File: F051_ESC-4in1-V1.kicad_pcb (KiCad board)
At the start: 4 copper layers, 41 x 40 mm, 136 parts, among them J1 Conn_01x02, J2 Conn_01x04, J3 Conn_01x04, J4 Conn_01x03, J5 Conn_01x04, J6 Conn_01x03, J7 Conn_01x03, J8 Conn_01x03, Q1 TPHR8504PL, Q10 TPHR8504PL, Q11 TPHR8504PL, Q12 TPHR8504PL, Q2 TPHR8504PL, Q3 TPHR8504PL, Q4 TPHR8504PL, Q5 TPHR8504PL, Q6 TPHR8504PL, Q7 TPHR8504PL, Q8 TPHR8504PL, Q9 TPHR8504PL, U1 FD6288Q, U2 STM32F051K6Ux, U3 L78L12_SOT89, U4 LP2985-3.3, U5 INA139, U6 FD6288Q, U7 OPA340NA, U8 STM32F051K6Ux

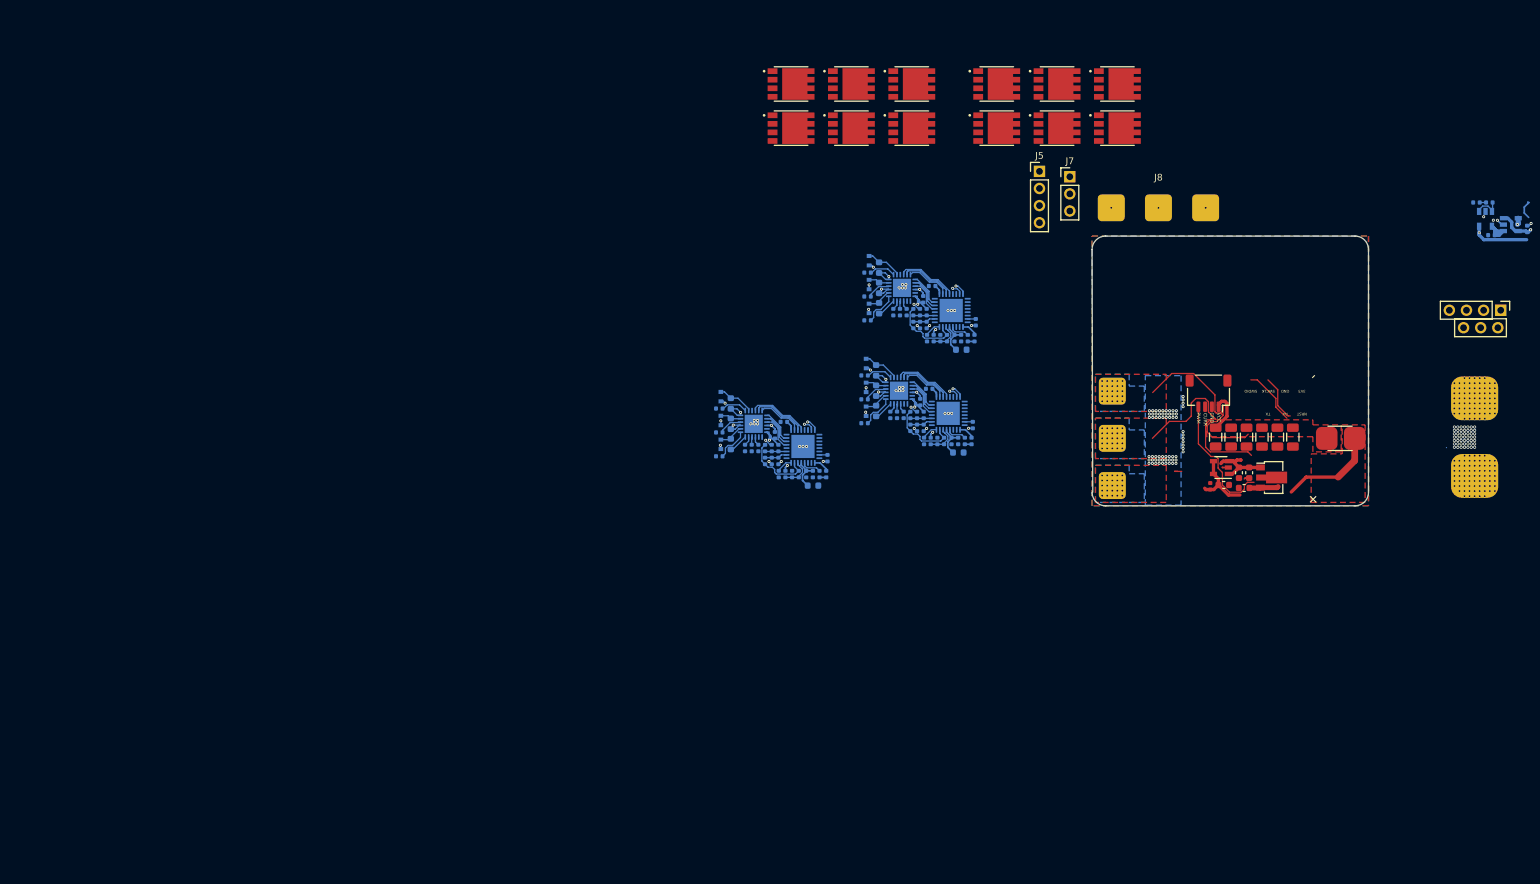
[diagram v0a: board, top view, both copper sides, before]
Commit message: Added the rest of the phases and their associated components
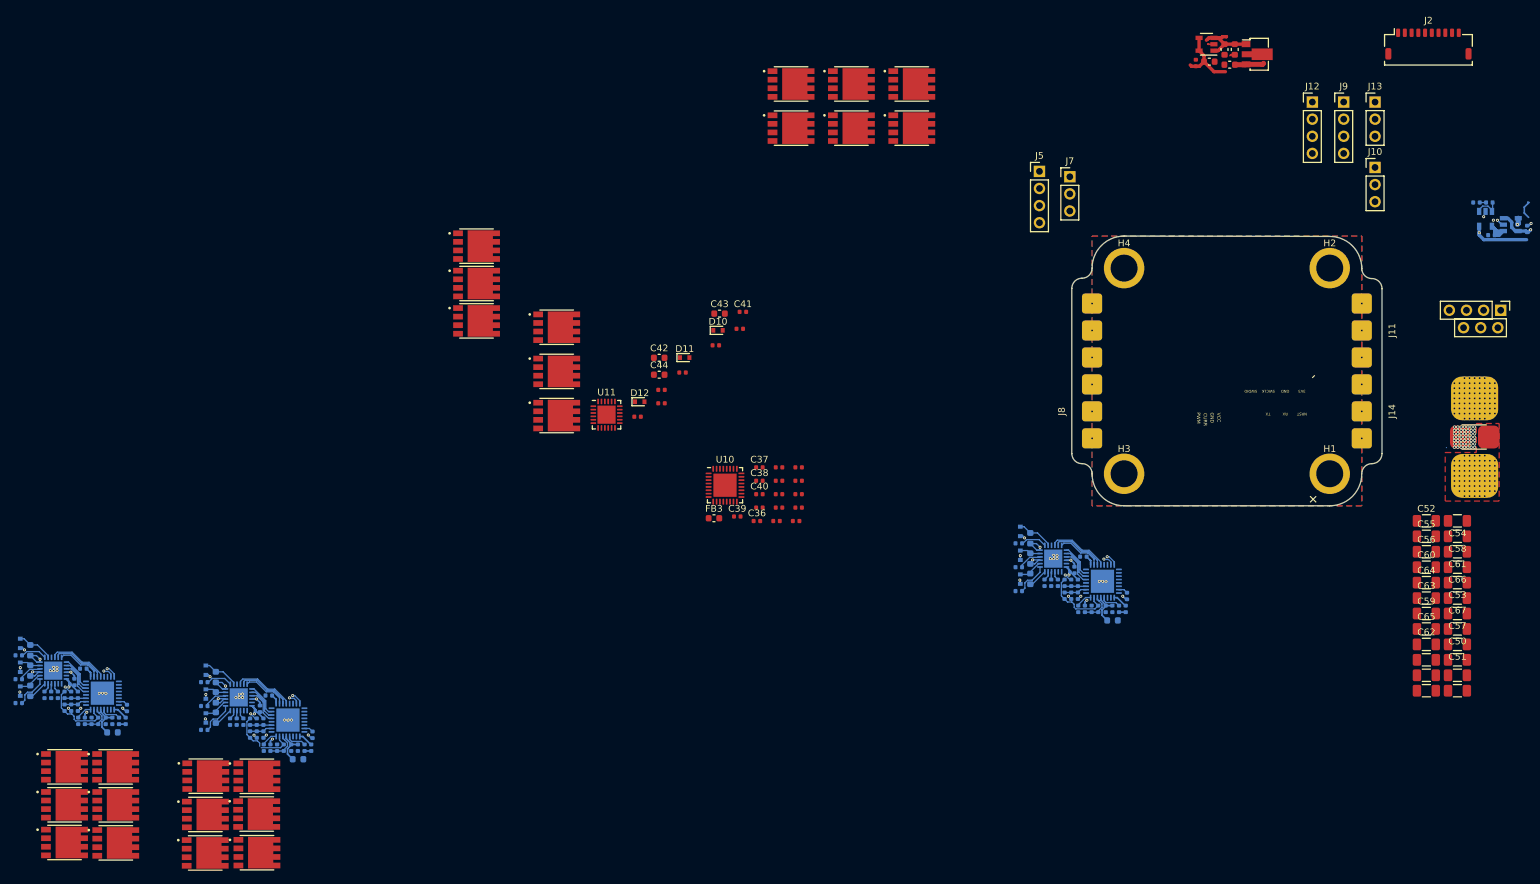
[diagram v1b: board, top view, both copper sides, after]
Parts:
- removed the C1 at (179.6, 85.3)
- removed the C11 at (172.0, 79.5)
- removed the C12 at (165.4, 77.8)
- removed the C13 at (165.4, 74.8)
- removed the C14 at (165.4, 80.8)
- removed the C15 at (178.6, 85.3)
- removed the C2 at (173.3, 77.6)
- removed the C3 at (176.6, 85.3)
- removed the C6 at (177.6, 85.3)
- removed the D2 at (163.9, 77.3)
- removed the D3 at (163.9, 73.8)
- removed the D4 at (163.9, 80.9)
- removed the FB1 at (177.6, 87.0)
- removed the R10 at (168.5, 81.4)
- removed the R11 at (163.7, 82.7)
- removed the R12 at (169.5, 81.4)
- removed the R13 at (171.5, 81.4)
- removed the R14 at (170.5, 81.4)
- removed the R15 at (171.5, 83.3)
- removed the R16 at (172.5, 81.4)
- removed the R17 at (170.5, 83.3)
- removed the R18 at (174.5, 85.3)
- removed the R19 at (175.5, 85.3)
- removed the R20 at (172.5, 83.3)
- removed the R21 at (173.5, 85.3)
- removed the R23 at (179.8, 82.9)
- removed the R24 at (172.5, 85.3)
- removed the R7 at (163.7, 75.6)
- removed the R8 at (167.5, 81.4)
- removed the R9 at (163.7, 79.1)
- removed the U1 at (168.8, 77.8)
- removed the U2 at (176.1, 81.2)
- added C32: 0.1uF, Capacitor_SMD:C_0402_1005Metric, B.Cu at (95.6, 120.1)
- added C33: 0.1uF, Capacitor_SMD:C_0603_1608Metric, B.Cu at (89.0, 115.4)
- added C34: 0.1uF, Capacitor_SMD:C_0603_1608Metric, B.Cu at (89.0, 118.4)
- added C35: 0.1uF, Capacitor_SMD:C_0603_1608Metric, B.Cu at (89.0, 121.4)
- added C36: 10nF, Capacitor_SMD:C_0402_1005Metric, F.Cu at (169.3, 92.3)
- added C37: 1uF, Capacitor_SMD:C_0402_1005Metric, F.Cu at (169.7, 84.3)
- added C38: 0.1uF, Capacitor_SMD:C_0402_1005Metric, F.Cu at (169.7, 86.3)
- added C39: 0.1uF, Capacitor_SMD:C_0402_1005Metric, F.Cu at (166.4, 91.6)
- added C40: 0.1uF, Capacitor_SMD:C_0402_1005Metric, F.Cu at (169.7, 88.3)
- added C41: 0.1uF, Capacitor_SMD:C_0402_1005Metric, F.Cu at (167.2, 61.2)
- added C42: 0.1uF, Capacitor_SMD:C_0603_1608Metric, F.Cu at (154.8, 68.0)
- added C43: 0.1uF, Capacitor_SMD:C_0603_1608Metric, F.Cu at (163.8, 61.5)
- added C44: 0.1uF, Capacitor_SMD:C_0603_1608Metric, F.Cu at (154.8, 70.6)
- added C45: 10nF, Capacitor_SMD:C_0402_1005Metric, B.Cu at (100.2, 125.9)
- added C46: 1uF, Capacitor_SMD:C_0402_1005Metric, B.Cu at (101.2, 125.9)
- added C47: 0.1uF, Capacitor_SMD:C_0402_1005Metric, B.Cu at (103.2, 125.9)
- added C48: 0.1uF, Capacitor_SMD:C_0402_1005Metric, B.Cu at (96.9, 118.1)
- added C49: 0.1uF, Capacitor_SMD:C_0402_1005Metric, B.Cu at (102.2, 125.9)
- added C50: 0.1uF, Capacitor_SMD:C_1206_3216Metric, F.Cu at (273.2, 108.3)
- added C51: 0.1uF, Capacitor_SMD:C_1206_3216Metric, F.Cu at (273.2, 110.6)
- added C52: 0.1uF, Capacitor_SMD:C_1206_3216Metric, F.Cu at (268.6, 92.2)
- added C53: 0.1uF, Capacitor_SMD:C_1206_3216Metric, F.Cu at (273.2, 101.4)
- added C54: 0.1uF, Capacitor_SMD:C_1206_3216Metric, F.Cu at (273.2, 92.2)
- added C55: 0.1uF, Capacitor_SMD:C_1206_3216Metric, F.Cu at (268.6, 94.5)
- added C56: 0.1uF, Capacitor_SMD:C_1206_3216Metric, F.Cu at (268.6, 96.8)
- added C57: 0.1uF, Capacitor_SMD:C_1206_3216Metric, F.Cu at (273.2, 106.0)
- added C58: 0.1uF, Capacitor_SMD:C_1206_3216Metric, F.Cu at (273.2, 94.5)
- added C59: 0.1uF, Capacitor_SMD:C_1206_3216Metric, F.Cu at (268.6, 106.0)
- added C60: 0.1uF, Capacitor_SMD:C_1206_3216Metric, F.Cu at (268.6, 99.1)
- added C61: 0.1uF, Capacitor_SMD:C_1206_3216Metric, F.Cu at (273.2, 96.8)
- added C62: 0.1uF, Capacitor_SMD:C_1206_3216Metric, F.Cu at (268.6, 110.6)
- added C63: 0.1uF, Capacitor_SMD:C_1206_3216Metric, F.Cu at (268.6, 103.7)
- added C64: 0.1uF, Capacitor_SMD:C_1206_3216Metric, F.Cu at (268.6, 101.4)
- added C65: 0.1uF, Capacitor_SMD:C_1206_3216Metric, F.Cu at (268.6, 108.3)
- added C66: 0.1uF, Capacitor_SMD:C_1206_3216Metric, F.Cu at (273.2, 99.1)
- added C67: 0.1uF, Capacitor_SMD:C_1206_3216Metric, F.Cu at (273.2, 103.7)
- added D10: 250V, Diode_SMD:D_SOD-523, F.Cu at (163.5, 64.0)
- added D11: 250V, Diode_SMD:D_SOD-523, F.Cu at (158.6, 68.0)
- added D12: 250V, Diode_SMD:D_SOD-523, F.Cu at (151.9, 74.6)
- added D7: 250V, Diode_SMD:D_SOD-523, B.Cu at (87.6, 114.4)
- added D8: 250V, Diode_SMD:D_SOD-523, B.Cu at (87.6, 117.9)
- added D9: 250V, Diode_SMD:D_SOD-523, B.Cu at (87.6, 121.5)
- added FB3: 100@100MHz, Inductor_SMD:L_0603_1608Metric, F.Cu at (162.9, 91.8)
- added FB4: 100@100MHz, Inductor_SMD:L_0603_1608Metric, B.Cu at (101.2, 127.6)
- added H1: MountingHole_Pad, MountingHole:MountingHole_2.7mm_Pad, F.Cu at (254.2, 85.2)
- added H2: MountingHole_Pad, MountingHole:MountingHole_2.7mm_Pad, F.Cu at (254.2, 54.8)
- added H3: MountingHole_Pad, MountingHole:MountingHole_2.7mm_Pad, F.Cu at (223.8, 85.2)
- added H4: MountingHole_Pad, MountingHole:MountingHole_2.7mm_Pad, F.Cu at (223.8, 54.8)
- added J10: Conn_01x03, Connector_PinHeader_2.54mm:PinHeader_1x03_P2.54mm_Vertical, F.Cu at (261.0, 39.8)
- added J11: Conn_01x03, Connector_Wire:Conn_MotorPhase, F.Cu at (259.0, 64.0)
- added J12: Conn_01x04, Connector_PinHeader_2.54mm:PinHeader_1x04_P2.54mm_Vertical, F.Cu at (251.7, 30.1)
- added J13: Conn_01x03, Connector_PinHeader_2.54mm:PinHeader_1x03_P2.54mm_Vertical, F.Cu at (261.0, 30.1)
- added J14: Conn_01x03, Connector_Wire:Conn_MotorPhase, F.Cu at (259.0, 76.0)
- added J9: Conn_01x04, Connector_PinHeader_2.54mm:PinHeader_1x04_P2.54mm_Vertical, F.Cu at (256.3, 30.1)
- added Q13: TPHR8504PL, Footprints:TPHR8504PL, F.Cu at (87.5, 141.5)
- added Q14: TPHR8504PL, Footprints:TPHR8504PL, F.Cu at (95.1, 141.4)
- added Q15: TPHR8504PL, Footprints:TPHR8504PL, F.Cu at (87.5, 135.8)
- added Q16: TPHR8504PL, Footprints:TPHR8504PL, F.Cu at (95.1, 135.7)
- added Q17: TPHR8504PL, Footprints:TPHR8504PL, F.Cu at (87.5, 130.1)
- added Q18: TPHR8504PL, Footprints:TPHR8504PL, F.Cu at (95.1, 130.1)
- added Q19: TPHR8504PL, Footprints:TPHR8504PL, F.Cu at (127.7, 51.5)
- added Q20: TPHR8504PL, Footprints:TPHR8504PL, F.Cu at (127.7, 62.6)
- added Q21: TPHR8504PL, Footprints:TPHR8504PL, F.Cu at (139.6, 76.6)
- added Q22: TPHR8504PL, Footprints:TPHR8504PL, F.Cu at (127.7, 57.0)
- added Q23: TPHR8504PL, Footprints:TPHR8504PL, F.Cu at (139.6, 70.1)
- added Q24: TPHR8504PL, Footprints:TPHR8504PL, F.Cu at (139.6, 63.5)
- added R38: 10, Resistor_SMD:R_0402_1005Metric, B.Cu at (87.3, 116.2)
- added R39: 10, Resistor_SMD:R_0402_1005Metric, B.Cu at (91.2, 122.0)
- added R40: 10, Resistor_SMD:R_0402_1005Metric, B.Cu at (87.3, 119.7)
- added R41: 10, Resistor_SMD:R_0402_1005Metric, B.Cu at (92.1, 122.0)
- added R42: 10, Resistor_SMD:R_0402_1005Metric, B.Cu at (87.3, 123.2)
- added R43: 10, Resistor_SMD:R_0402_1005Metric, B.Cu at (93.1, 122.0)
- added R44: 10k, Resistor_SMD:R_0402_1005Metric, F.Cu at (172.6, 86.3)
- added R45: 10k, Resistor_SMD:R_0402_1005Metric, F.Cu at (172.6, 88.3)
- added R46: 10k, Resistor_SMD:R_0402_1005Metric, F.Cu at (175.5, 86.3)
- added R47: 10k, Resistor_SMD:R_0402_1005Metric, F.Cu at (175.1, 92.3)
- added R48: 1k, Resistor_SMD:R_0402_1005Metric, F.Cu at (175.5, 88.3)
- added R49: 10k, Resistor_SMD:R_0402_1005Metric, F.Cu at (172.6, 90.3)
- added R50: 10k, Resistor_SMD:R_0402_1005Metric, F.Cu at (175.5, 90.3)
- added R51: 1k, Resistor_SMD:R_0402_1005Metric, F.Cu at (172.2, 92.3)
- added R52: 1k, Resistor_SMD:R_0402_1005Metric, F.Cu at (169.7, 90.3)
- added R53: 1k, Resistor_SMD:R_0402_1005Metric, F.Cu at (175.5, 84.3)
- added R54: 1k, Resistor_SMD:R_0402_1005Metric, F.Cu at (172.6, 84.3)
- added R55: 10, Resistor_SMD:R_0402_1005Metric, F.Cu at (155.1, 72.8)
- added R56: 10, Resistor_SMD:R_0402_1005Metric, F.Cu at (163.2, 66.2)
- added R57: 10, Resistor_SMD:R_0402_1005Metric, F.Cu at (166.8, 63.8)
- added R58: 10, Resistor_SMD:R_0402_1005Metric, F.Cu at (155.1, 74.8)
- added R59: 10, Resistor_SMD:R_0402_1005Metric, F.Cu at (158.3, 70.2)
- added R60: 10, Resistor_SMD:R_0402_1005Metric, F.Cu at (151.6, 76.8)
- added R61: 10k, Resistor_SMD:R_0402_1005Metric, B.Cu at (95.1, 122.0)
- added R62: 10k, Resistor_SMD:R_0402_1005Metric, B.Cu at (94.1, 122.0)
- added R63: 10k, Resistor_SMD:R_0402_1005Metric, B.Cu at (95.1, 123.9)
- added R64: 10k, Resistor_SMD:R_0402_1005Metric, B.Cu at (94.1, 123.9)
- added R65: 1k, Resistor_SMD:R_0402_1005Metric, B.Cu at (96.2, 125.9)
- added R66: 10k, Resistor_SMD:R_0402_1005Metric, B.Cu at (98.1, 125.9)
- added R67: 10k, Resistor_SMD:R_0402_1005Metric, B.Cu at (99.1, 125.9)
- added R68: 1k, Resistor_SMD:R_0402_1005Metric, B.Cu at (96.1, 122.0)
- added R69: 1k, Resistor_SMD:R_0402_1005Metric, B.Cu at (96.1, 123.9)
- added R70: 1k, Resistor_SMD:R_0402_1005Metric, B.Cu at (97.1, 125.9)
- added R71: 1k, Resistor_SMD:R_0402_1005Metric, B.Cu at (103.4, 124.0)
- added U10: STM32F051K6Ux, Package_DFN_QFN:QFN-32-1EP_5x5mm_P0.5mm_EP3.45x3.45mm, F.Cu at (164.6, 87.0)
- added U11: FD6288Q, Package_DFN_QFN:QFN-24-1EP_4x4mm_P0.5mm_EP2.7x2.7mm, F.Cu at (147.0, 76.5)
- added U12: STM32F051K6Ux, Package_DFN_QFN:QFN-32-1EP_5x5mm_P0.5mm_EP3.45x3.45mm, B.Cu at (99.7, 121.8)
- added U9: FD6288Q, Package_DFN_QFN:QFN-24-1EP_4x4mm_P0.5mm_EP2.7x2.7mm, B.Cu at (92.4, 118.4)
- J2: value Conn_01x04 -> Conn_01x10; footprint Connector_JST:JST_SH_SM04B-SRSS-TB_1x04-1MP_P1.00mm_Horizontal -> Connector_JST:JST_SHL_SM10B-SHLS-TF_1x10-1MP_P1.00mm_Horizontal
- moved Q11 186.1 mm to (66.6, 128.7)
- moved Q9 181.9 mm to (66.6, 134.3)
- moved Q7 178.2 mm to (66.6, 139.9)
- moved Q12 176.2 mm to (74.2, 128.7)
- moved Q10 171.9 mm to (74.2, 134.4)
- moved Q8 168.3 mm to (74.2, 140.0)
- moved R37 138.3 mm to (75.9, 120.0)
- moved C27 138.1 mm to (73.7, 121.9)
- moved D1 138.1 mm to (60.0, 110.4)
- moved D5 138.1 mm to (60.0, 114.0)
- moved D6 138.1 mm to (60.0, 117.5)
- moved R28 138.1 mm to (66.6, 118.0)
- moved R30 138.1 mm to (66.6, 120.0)
- moved R31 138.1 mm to (68.6, 121.9)
- moved R33 138.1 mm to (71.6, 121.9)
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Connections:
- net /FET Driver 2/HIN1 renamed /MOSFET Driver 2/HIN1
- net /FET Driver 2/HIN2 renamed /MCU 2/HIN2
- net /FET Driver 2/HO1 renamed /MOSFET Driver 2/HO1
- net /FET Driver 2/HO2 renamed /MOSFET Driver 2/HO2
- net /FET Driver 2/HO3 renamed /MOSFET Driver 2/HO3
- net /FET Driver 2/LIN1 renamed /MCU 2/LIN1
- net /FET Driver 2/LIN2 renamed /MCU 2/LIN2
- net /FET Driver 2/LIN3 renamed /MCU 2/LIN3
- net /FET Driver 2/LO1 renamed /MOSFET Driver 2/LO1
- net /FET Driver 2/LO2 renamed /MOSFET Driver 2/LO2
- net /FET Driver 2/LO3 renamed /MOSFET Driver 2/LO3
- net /FET Driver 2/PhaseA renamed /MCU 2/PhaseA
- net /FET Driver 2/PhaseB renamed /MCU 2/PhaseB
- net /FET Driver 2/PhaseC renamed /MCU 2/PhaseC
- net /FET Driver 2/VB1 renamed /MOSFET Driver 2/VB1
- net /FET Driver 2/VB2 renamed /MOSFET Driver 2/VB2
- net /FET Driver 2/VB3 renamed /MOSFET Driver 2/VB3
- J2 pad 3: /Curent Sense/CURR -> (no net)
- J2 pad 4: (no net) -> GND
- R24 pad 2: /MCU 1/PWM -> /PWM_1
- R31 pad 2: (no net) -> /PWM_2
- U2 pad 12: Net-(U2-Pad12) -> (no net)
- U2 pad 16: Net-(U2-Pad16) -> (no net)
- U2 pad 2: Net-(U2-Pad2) -> (no net)
- U2 pad 21: Net-(U2-Pad21) -> (no net)
- U2 pad 22: Net-(U2-Pad22) -> (no net)
- U2 pad 25: Net-(U2-Pad25) -> (no net)
- U2 pad 26: Net-(U2-Pad26) -> (no net)
- U2 pad 27: Net-(U2-Pad27) -> (no net)
- U2 pad 28: Net-(U2-Pad28) -> (no net)
- U2 pad 3: Net-(U2-Pad3) -> (no net)
- U2 pad 32: Net-(U2-Pad32) -> (no net)
- U2 pad 9: Net-(U2-Pad9) -> (no net)
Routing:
- net /MCU 1/PhaseA: track 39.0 -> 5.14 mm, vias 28 -> 2
- net /MCU 1/PhaseB: track 35.8 -> 4.08 mm, vias 28 -> 2
- net (no net): track 19.6 -> 39.3 mm
- net VCC: track 20.1 -> 5.49 mm
- net /MCU 1/SenseCOM: track 21.6 -> 10.8 mm
- net /MCU 4/SenseCOM: track 0.00 -> 10.5 mm
- net /MCU 1/SWDIO: track 11.7 -> 1.64 mm, vias 2 -> 1
- net /MOSFET Driver 1/HIN1: track 18.2 -> 9.12 mm
- net /MCU 1/SWCLK: track 10.5 -> 1.80 mm, vias 2 -> 1
- net +12V: track 29.4 -> 21.2 mm
- net /MCU 1/HIN2: track 16.1 -> 8.07 mm
- net /MCU 1/HIN1: track 13.5 -> 6.75 mm
- net VCC_Shunt: track 11.5 -> 5.32 mm, vias 104 -> 50
- net /MOSFET Driver 1/VB1: track 10.9 -> 5.43 mm
- net /MOSFET Driver 3/VB1: track 0.00 -> 5.43 mm
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- removed copper zone on In2.Cu, net +12V
- removed copper zone on B.Cu, net /MCU 1/PhaseA
- removed copper zone on F.Cu, net /MCU 1/PhaseA
- removed copper zone on B.Cu, net /MCU 1/PhaseB
- removed copper zone on F.Cu, net /MCU 1/PhaseB
- removed copper zone on B.Cu, net /MCU 1/PhaseC
- removed copper zone on F.Cu, net /MCU 1/PhaseC
- removed copper zone on B.Cu, net VCC_Shunt
- removed copper zone on F.Cu, net VCC_Shunt
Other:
- board size 41 x 40 mm -> 46 x 40 mm

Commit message: Updated Design
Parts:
- C36, C37, C38, C39, C40, C41, C42, C43, C44, D10, D11, D12, FB3, R44, R45, R46, R47, R48, R49, R50, R51, R52, R53, R54, R55, R56, R57, R58, R59, R60, U10, U11: moved to B.Cu
- moved R42 135.3 mm to (205.1, 56.7), turned to 180 degrees
- moved D9 133.2 mm to (204.9, 58.4), turned to 90 degrees
- moved R40 132.0 mm to (205.1, 60.2), turned to 180 degrees
- moved C35 130.5 mm to (203.4, 58.5), turned to 90 degrees
- moved D8 130.0 mm to (204.9, 62.0), turned to 90 degrees
- moved R38 128.9 mm to (205.1, 63.8), turned to 180 degrees
- moved C34 127.7 mm to (203.4, 61.5), turned to 90 degrees
- moved R39 127.4 mm to (201.3, 57.9), turned to 270 degrees
- moved D7 127.1 mm to (204.9, 65.5), turned to 90 degrees
- moved R41 125.7 mm to (200.3, 57.9), turned to 270 degrees
- moved C33 125.2 mm to (203.4, 64.5), turned to 90 degrees
- moved R43 124.0 mm to (199.3, 57.9), turned to 270 degrees
- moved U9 121.7 mm to (200.0, 61.5), turned to 0 degrees
- moved D1 120.8 mm to (173.2, 68.3)
- moved D5 120.8 mm to (173.2, 71.8)
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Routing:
- net (no net): track 39.3 -> 0.00 mm
- net /MCU 3/SenseCOM: track 0.00 -> 9.88 mm
- net /MOSFET Driver 4/HIN1: track 0.00 -> 9.12 mm
- net /MOSFET Driver 3/HIN1: track 0.00 -> 9.12 mm
- net /MCU 3/HIN2: track 0.00 -> 8.07 mm
- net /MCU 4/HIN2: track 0.00 -> 8.07 mm
- net /MCU 4/HIN1: track 0.00 -> 6.75 mm
- net /MCU 3/HIN1: track 0.00 -> 6.49 mm
- net GND: track 27.9 -> 33.4 mm, vias 111 -> 119
- net /MOSFET Driver 4/VB1: track 0.00 -> 5.43 mm
- net /MOSFET Driver 4/HO3: track 0.00 -> 5.29 mm
- net /MCU 4/LIN3: track 0.00 -> 5.25 mm
- net /MCU 3/LIN3: track 0.00 -> 5.25 mm
- net /MCU 4/LIN2: track 0.00 -> 5.12 mm
- net /MCU 3/LIN2: track 0.00 -> 5.12 mm
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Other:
- board text added: "1"
- board text added: "2"
- board text added: "3"
- board text added: "4"

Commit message: Added a test circuit to figure out best configuration
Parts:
- added C68: 0.1uF, Capacitor_SMD:C_0402_1005Metric, B.Cu at (43.0, 91.5)
- added C69: 0.1uF, Capacitor_SMD:C_0603_1608Metric, B.Cu at (35.8, 88.4)
- added C70: 0.1uF, Capacitor_SMD:C_0603_1608Metric, B.Cu at (35.8, 91.3)
- added C71: 0.1uF, Capacitor_SMD:C_0603_1608Metric, B.Cu at (35.8, 94.3)
- added C72: 10nF, Capacitor_SMD:C_0402_1005Metric, B.Cu at (39.6, 81.2)
- added C73: 1uF, Capacitor_SMD:C_0402_1005Metric, B.Cu at (39.6, 80.2)
- added C74: 0.1uF, Capacitor_SMD:C_0402_1005Metric, B.Cu at (37.2, 80.7)
- added C75: 0.1uF, Capacitor_SMD:C_0402_1005Metric, B.Cu at (43.2, 88.2)
- added C76: 0.1uF, Capacitor_SMD:C_0402_1005Metric, B.Cu at (38.2, 80.7)
- added D13: 250V, Diode_SMD:D_SOD-523, B.Cu at (36.0, 86.9)
- added D14: 250V, Diode_SMD:D_SOD-523, B.Cu at (36.0, 89.8)
- added D15: 250V, Diode_SMD:D_SOD-523, B.Cu at (36.0, 92.8)
- added FB5: 100@100MHz, Inductor_SMD:L_0603_1608Metric, B.Cu at (39.1, 79.0)
- added J15: Conn_01x04, Connector_PinHeader_2.54mm:PinHeader_1x04_P2.54mm_Vertical, F.Cu at (106.3, 88.7)
- added J16: Conn_01x03, Connector_PinHeader_2.54mm:PinHeader_1x03_P2.54mm_Vertical, F.Cu at (110.9, 88.7)
- added J17: Conn_01x03, Connector_Wire:Conn_MotorPhase, F.Cu at (97.4, 89.0)
- added Q25: TPHR8504PL, Footprints:TPHR8504PL, F.Cu at (95.5, 66.6)
- added Q26: TPHR8504PL, Footprints:TPHR8504PL, F.Cu at (95.5, 73.2)
- added Q27: TPHR8504PL, Footprints:TPHR8504PL, F.Cu at (104.5, 66.6)
- added Q28: TPHR8504PL, Footprints:TPHR8504PL, F.Cu at (95.5, 79.7)
- added Q29: TPHR8504PL, Footprints:TPHR8504PL, F.Cu at (104.5, 73.2)
- added Q30: TPHR8504PL, Footprints:TPHR8504PL, F.Cu at (113.4, 66.6)
- added R72: 10, Resistor_SMD:R_0402_1005Metric, B.Cu at (34.2, 89.8)
- added R73: 10, Resistor_SMD:R_0402_1005Metric, B.Cu at (37.8, 94.2)
- added R74: 10, Resistor_SMD:R_0402_1005Metric, B.Cu at (34.2, 92.8)
- added R75: 10, Resistor_SMD:R_0402_1005Metric, B.Cu at (38.7, 94.2)
- added R76: 10, Resistor_SMD:R_0402_1005Metric, B.Cu at (34.2, 95.8)
- added R77: 10, Resistor_SMD:R_0402_1005Metric, B.Cu at (39.7, 94.2)
- added R78: 10k, Resistor_SMD:R_0402_1005Metric, B.Cu at (44.5, 85.2)
- added R79: 10k, Resistor_SMD:R_0402_1005Metric, B.Cu at (44.5, 83.2)
- added R80: 10k, Resistor_SMD:R_0402_1005Metric, B.Cu at (44.5, 82.3)
- added R81: 10k, Resistor_SMD:R_0402_1005Metric, B.Cu at (44.5, 80.3)
- added R82: 1k, Resistor_SMD:R_0402_1005Metric, B.Cu at (44.5, 79.3)
- added R83: 10k, Resistor_SMD:R_0402_1005Metric, B.Cu at (41.1, 80.7)
- added R84: 10k, Resistor_SMD:R_0402_1005Metric, B.Cu at (43.0, 80.7)
- added R85: 1k, Resistor_SMD:R_0402_1005Metric, B.Cu at (44.5, 84.2)
- added R86: 1k, Resistor_SMD:R_0402_1005Metric, B.Cu at (44.5, 81.3)
- added R87: 1k, Resistor_SMD:R_0402_1005Metric, B.Cu at (42.1, 80.7)
- added R88: 1k, Resistor_SMD:R_0402_1005Metric, B.Cu at (36.8, 82.7)
- added U13: FD6288Q, Package_DFN_QFN:QFN-24-1EP_4x4mm_P0.5mm_EP2.7x2.7mm, B.Cu at (39.9, 90.6)
- added U14: STM32F051K6Ux, Package_DFN_QFN:QFN-32-1EP_5x5mm_P0.5mm_EP3.45x3.45mm, B.Cu at (40.4, 84.8)
- Q10, Q14, Q16, Q22, Q24, Q4, Q6, Q8: moved to B.Cu
- moved R28 138.4 mm to (41.5, 71.1)
- moved R30 138.4 mm to (41.5, 73.0)
- moved R5 138.4 mm to (38.5, 71.1)
- moved C10 138.4 mm to (36.4, 64.5)
- moved C25 138.4 mm to (36.4, 67.5)
- moved C26 138.4 mm to (36.4, 70.5)
- moved C27 138.4 mm to (48.6, 75.0)
- moved C28 138.4 mm to (47.6, 75.0)
- moved C29 138.4 mm to (50.5, 75.0)
- moved C30 138.4 mm to (44.3, 67.2)
- moved C31 138.4 mm to (49.6, 75.0)
- moved C9 138.4 mm to (42.9, 69.2)
- moved D1 138.4 mm to (34.9, 63.5)
- moved D5 138.4 mm to (34.9, 67.0)
- moved D6 138.4 mm to (34.9, 70.6)
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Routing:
- net /MCU Test/SenseCOM: track 0.00 -> 9.59 mm
- net /MCU Test/LIN3: track 0.00 -> 7.44 mm
- net /MCU Test/LIN2: track 0.00 -> 6.51 mm
- net /MOSFET Driver Test/VB1: track 0.00 -> 6.46 mm
- net /MOSFET Driver Test/HO3: track 0.00 -> 6.31 mm
- net /MOSFET Driver Test/HO1: track 0.00 -> 5.74 mm
- net /MCU Test/LIN1: track 0.00 -> 5.47 mm
- net /MOSFET Driver Test/VB3: track 0.00 -> 5.12 mm
- net /MOSFET Driver Test/HO2: track 0.00 -> 4.89 mm
- net /MOSFET Driver Test/VB2: track 0.00 -> 4.70 mm
- net /MCU Test/SenseB: track 0.00 -> 4.05 mm
- net /MCU Test/PhaseC: track 0.00 -> 3.37 mm
- net /MCU Test/SenseA: track 0.00 -> 3.22 mm
- net +3V3: track 33.2 -> 36.4 mm
- net /MCU Test/SenseC: track 0.00 -> 3.19 mm
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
